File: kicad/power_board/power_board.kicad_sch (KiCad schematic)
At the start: 38 parts, among them J1 24V, J2 5V, J3 3V3, J4 GND, Q1 NTBGS1D5N06C, Q2 FDB13AN06A0, Q3 NTBGS1D5N06C, Q4 FDB13AN06A0, U1 LM2575D2T-3.3R4G, U2 LM2575D2T-5R4G, U3 LTC4359, U4 LTC4359

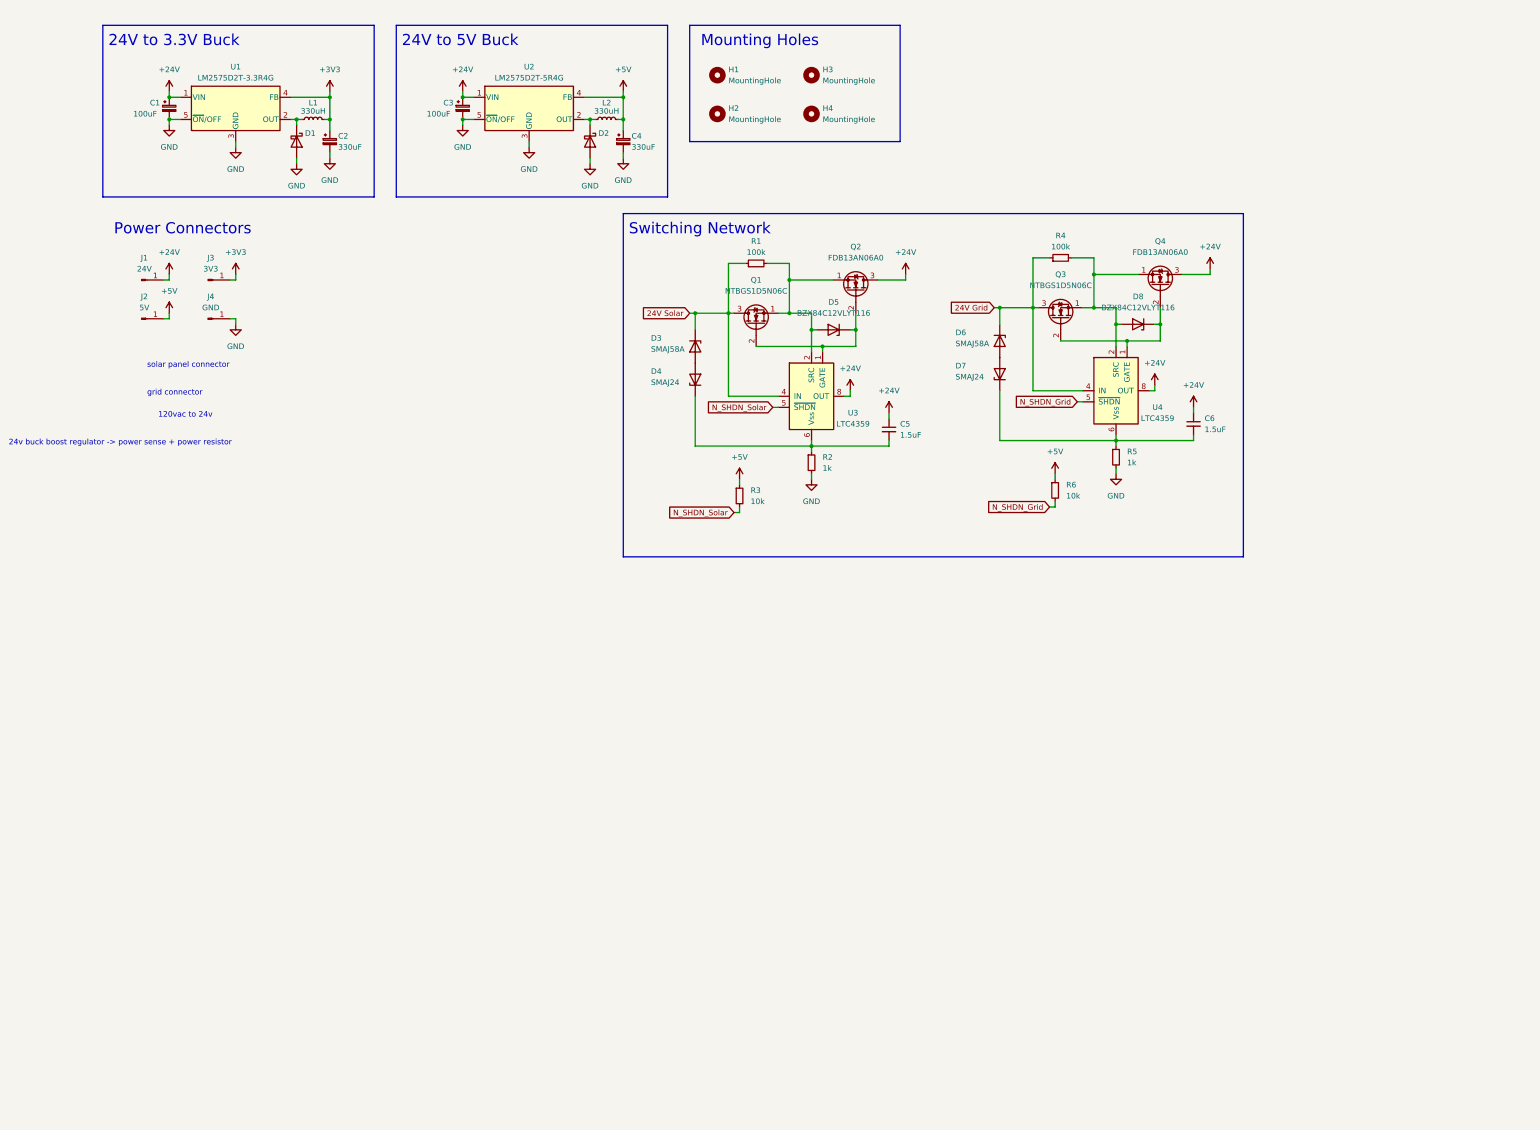
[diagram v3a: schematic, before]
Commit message: power board pcb
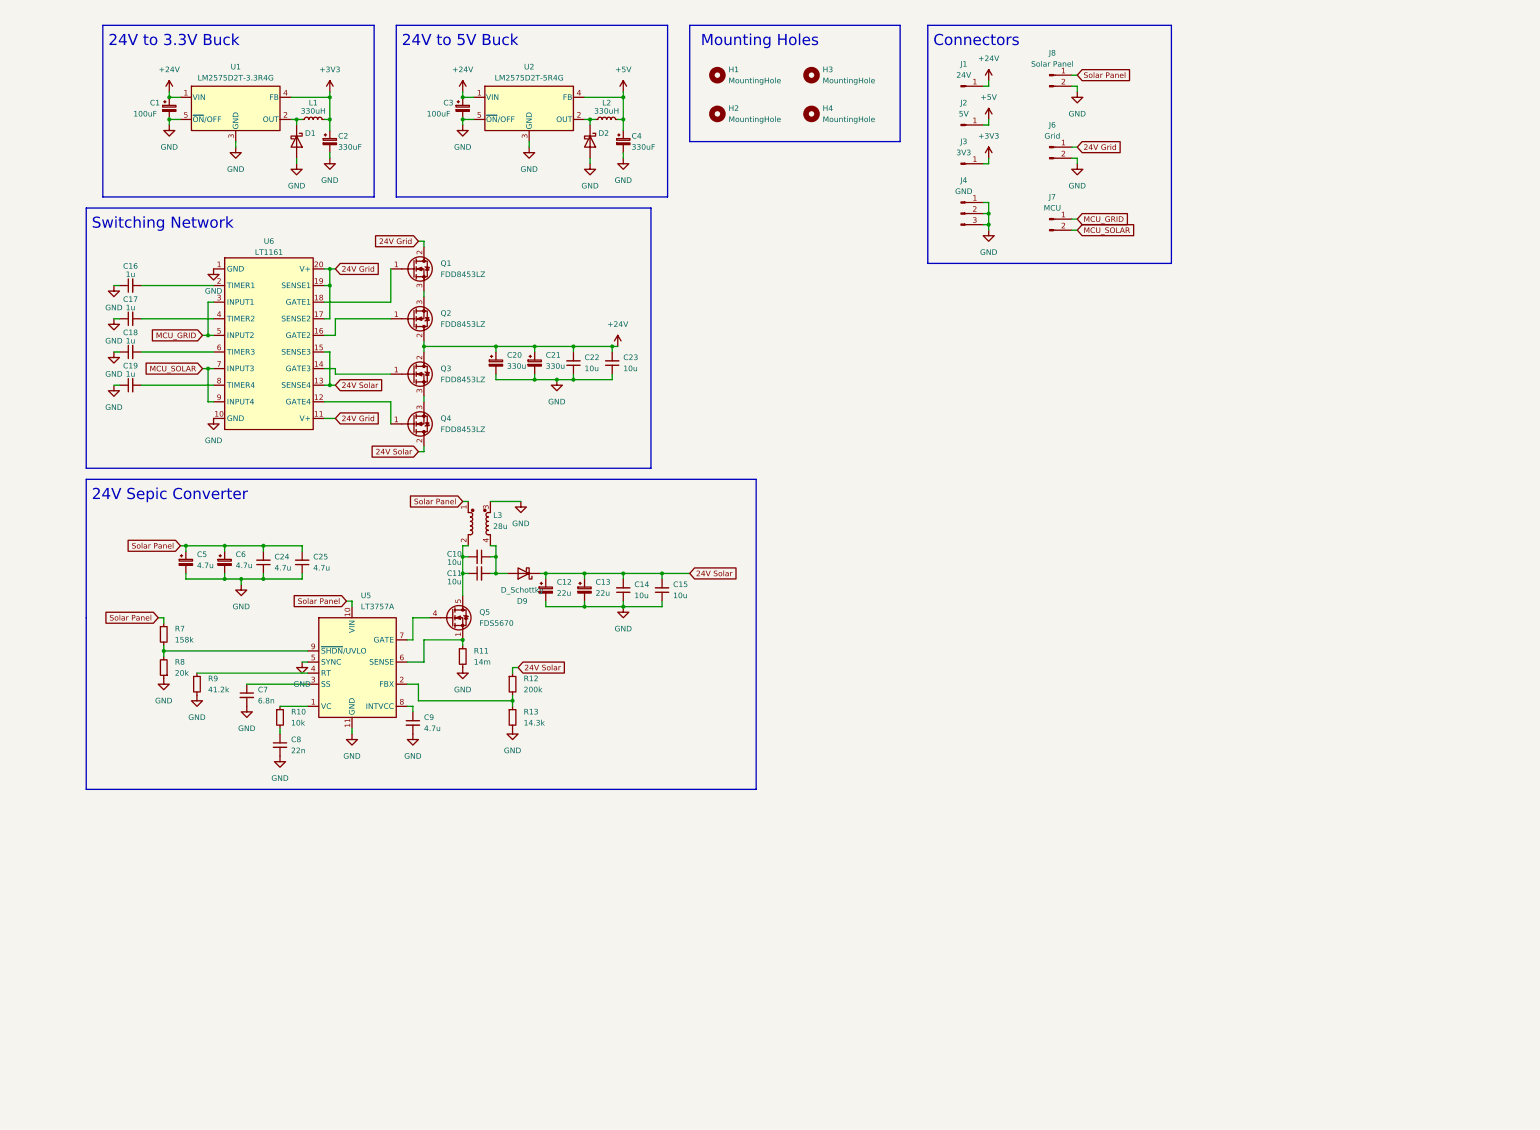
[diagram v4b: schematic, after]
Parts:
- removed C5, C6: 1.5uF, symbol Device:C_Small
- removed D3, D6: SMAJ58A, symbol Device:D_Zener
- removed D4, D7: SMAJ24, symbol Device:D_Zener
- removed D5, D8: BZX84C12VLYT116, symbol Device:D_Zener
- removed J4: GND, symbol Connector:Conn_01x01_Male
- removed Q1, Q3: NTBGS1D5N06C, Package_TO_SOT_THT:TO-92_Inline, symbol Transistor_FET:2N7000
- removed Q2, Q4: FDB13AN06A0, Package_TO_SOT_THT:TO-92_Inline, symbol Transistor_FET:2N7000
- removed R1, R4: 100k, symbol Device:R_Small
- removed R2, R5: 1k, symbol Device:R_Small
- removed R3, R6: 10k, symbol Device:R_Small
- removed U3, U4: LTC4359, Package_SO:MSOP-8_3x3mm_P0.65mm, symbol Power_Management:LTC4359-MS8
- added C10, C11, C14, C15, C22, C23: 10u, Capacitor_SMD:C_1210_3225Metric, symbol Device:C_Small
- added C12, C13: 22u, Capacitor_THT:CP_Radial_D5.0mm_P2.50mm, symbol Device:C_Polarized_Small
- added C16, C17, C18, C19: 1u, Capacitor_SMD:C_0603_1608Metric, symbol Device:C_Small
- added C20, C21: 330u, Capacitor_THT:C_Radial_D16.0mm_H25.0mm_P7.50mm, symbol Device:C_Polarized_Small
- added C24, C25: 4.7u, Capacitor_SMD:C_1210_3225Metric, symbol Device:C_Small
- added C5, C6: 4.7u, Capacitor_THT:CP_Radial_D5.0mm_P2.00mm, symbol Device:C_Polarized_Small
- added C7: 6.8n, Capacitor_SMD:C_0603_1608Metric, symbol Device:C_Small
- added C8: 22n, Capacitor_SMD:C_0603_1608Metric, symbol Device:C_Small
- added C9: 4.7u, Capacitor_SMD:C_0805_2012Metric, symbol Device:C_Small
- added D9: D_Schottky, Package_TO_SOT_SMD:TO-252-2, symbol Device:D_Schottky
- added J4: GND, Connector_PinHeader_2.54mm:PinHeader_1x03_P2.54mm_Vertical, symbol Connector:Conn_01x03_Male
- added J6: Grid, Connector_PinHeader_2.54mm:PinHeader_1x02_P2.54mm_Vertical, symbol Connector:Conn_01x02_Male
- added J7: MCU, Connector_PinHeader_2.54mm:PinHeader_1x02_P2.54mm_Vertical, symbol Connector:Conn_01x02_Male
- added J8: Solar Panel, Connector_PinHeader_2.54mm:PinHeader_1x02_P2.54mm_Vertical, symbol Connector:Conn_01x02_Male
- added L3: 28u, _mine:PF0553NL, symbol Device:L_Coupled
- added Q1, Q2, Q3, Q4: FDD8453LZ, Package_TO_SOT_SMD:TO-252-2, symbol Transistor_FET:BSP89
- added Q5: FDS5670, Package_TO_SOT_SMD:LFPAK33, symbol Transistor_FET:BUK7M6R3-40EX
- added R10: 10k, Resistor_SMD:R_0603_1608Metric, symbol Device:R_Small
- added R11: 14m, Resistor_SMD:R_2512_6332Metric, symbol Device:R_Small
- added R12: 200k, Resistor_SMD:R_1206_3216Metric, symbol Device:R_Small
- added R13: 14.3k, Resistor_SMD:R_0603_1608Metric, symbol Device:R_Small
- added R7: 158k, Resistor_SMD:R_0603_1608Metric, symbol Device:R_Small
- added R8: 20k, Resistor_SMD:R_0603_1608Metric, symbol Device:R_Small
- added R9: 41.2k, Resistor_SMD:R_0603_1608Metric, symbol Device:R_Small
- added U5: LT3757A, Package_SO:MSOP-10-1EP_3x3mm_P0.5mm_EP1.68x1.88mm, symbol Regulator_Switching:LT3757AEMSE
- added U6: LT1161, Package_SO:SOIC-20W_7.5x12.8mm_P1.27mm, symbol Driver_FET:HIP4080A
- C1, C3: footprint (none) -> Capacitor_THT:C_Radial_D8.0mm_H11.5mm_P3.50mm
- C2, C4: footprint (none) -> Capacitor_THT:CP_Radial_D8.0mm_P3.50mm
- D1, D2: footprint (none) -> Package_TO_SOT_SMD:TO-252-2
- H1, H2, H3, H4: footprint (none) -> MountingHole:MountingHole_3.5mm
- J1, J2, J3: footprint (none) -> Connector_PinHeader_2.54mm:PinHeader_1x01_P2.54mm_Vertical
- L1, L2: footprint (none) -> Inductor_THT:L_Toroid_Vertical_L31.8mm_W15.9mm_P13.50mm_Bourns_5700
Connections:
- net +24V: now also C20.1, C21.1, C22.2, C23.2, Q2.2 (D), Q3.2 (D)
- net 24V Grid: now also J6.1 (Pin_1), Q1.2 (D), U6.11 (V+), U6.17 (SENSE2), U6.19 (SENSE1), U6.20 (V+)
- net 24V Solar: now also C12.1, C13.1, C14.2, C15.2, D9.2 (K), Q4.2 (D), R12.1, U6.13 (SENSE4), U6.15 (SENSE3)
- net GND: now also C12.2, C13.2, C14.1, C15.1, C16.1, C17.1, C18.1, C19.1, C20.2, C21.2, C22.1, C23.1, C24.1, C25.1, C5.2, C6.2, C7.2, C8.2, C9.2, J4.1 (Pin_1), J4.2 (Pin_2), J4.3 (Pin_3), J6.2 (Pin_2), J8.2 (Pin_2), L3.3, R11.2, R13.2, R8.1, R9.2, U5.11 (GND), U5.5 (SYNC), U6.1 (GND), U6.10 (GND)
- new net: R7.2, R8.2, U5.9 (~{SHDN}/UVLO)
- new net: C9.1, U5.8 (INTVCC)
- new net: C10.1, C11.2, D9.1 (A), L3.4
- new net: C10.2, C11.1, L3.2, Q5.5 (D)
- new net: Q5.1 (S), Q5.2 (S), Q5.3 (S), R11.1, U5.6 (SENSE)
- new net: Q5.4 (G), U5.7 (GATE)
- new net: Q1.1 (G), U6.18 (GATE1)
- new net: Q1.3 (S), Q2.3 (S)
- new net: C16.2, U6.2 (TIMER1)
- new net: Q4.1 (G), U6.12 (GATE4)
- new net: Q3.1 (G), U6.14 (GATE3)
- new net: Q2.1 (G), U6.16 (GATE2)
- new net: C17.2, U6.4 (TIMER2)
- new net: C18.2, U6.6 (TIMER3)
- new net: C19.2, U6.8 (TIMER4)
- new net: Q3.3 (S), Q4.3 (S)
- new net: R9.1, U5.4 (RT)
- new net: C7.1, U5.3 (SS)
- new net: R12.2, R13.1, U5.2 (FBX)
- new net: R10.1, U5.1 (VC)
- new net: C8.1, R10.2
- new net MCU_GRID: J7.1 (Pin_1), U6.3 (INPUT1), U6.5 (INPUT2)
- new net MCU_SOLAR: J7.2 (Pin_2), U6.7 (INPUT3), U6.9 (INPUT4)
- new net Solar Panel: C24.2, C25.2, C5.1, C6.1, J8.1 (Pin_1), L3.1, R7.1, U5.10 (VIN)
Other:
- note added: "24V Sepic Converter"
- note added: "Connectors"
- note removed: "120vac to 24v"
- note removed: "24v buck boost regulator -> power sense + power resistor"
- note removed: "Power Connectors"
- note removed: "grid connector"
- note removed: "solar panel connector"
- moved on the sheet: J1, J2, J3

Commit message: traffic lights WIP
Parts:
- removed C1, C3: 100uF, Capacitor_THT:C_Radial_D8.0mm_H11.5mm_P3.50mm, symbol Device:C_Polarized_Small
- removed C2, C4: 330uF, Capacitor_THT:CP_Radial_D8.0mm_P3.50mm, symbol Device:C_Polarized_Small
- removed D1, D2: VS-30WQ04FNTR-M3, Package_TO_SOT_SMD:TO-252-2, symbol Device:D_Schottky
- removed J4: GND, Connector_PinHeader_2.54mm:PinHeader_1x03_P2.54mm_Vertical, symbol Connector:Conn_01x03_Male
- removed J6: Grid, Connector_PinHeader_2.54mm:PinHeader_1x02_P2.54mm_Vertical, symbol Connector:Conn_01x02_Male
- removed J8: Solar Panel, Connector_PinHeader_2.54mm:PinHeader_1x02_P2.54mm_Vertical, symbol Connector:Conn_01x02_Male
- removed L1, L2: 330uH, Inductor_THT:L_Toroid_Vertical_L31.8mm_W15.9mm_P13.50mm_Bourns_5700, symbol Device:L_Small
- removed U1: LM2575D2T-3.3R4G, Package_TO_SOT_SMD:TO-263-5_TabPin3, symbol Regulator_Switching:LM2575-3.3BU
- removed U2: LM2575D2T-5R4G, Package_TO_SOT_SMD:TO-263-5_TabPin3, symbol Regulator_Switching:LM2575-5.0BU
- added D1: LED, Capacitor_SMD:C_0603_1608Metric, symbol Device:LED
- added J10: Grid, Connector_PinHeader_2.54mm:PinHeader_1x01_P2.54mm_Vertical, symbol Connector:Conn_01x01_Male
- added J11: 24V Solar, Connector_PinHeader_2.54mm:PinHeader_1x01_P2.54mm_Vertical, symbol Connector:Conn_01x01_Male
- added J4, J5, J6: GND, Connector_PinHeader_2.54mm:PinHeader_1x01_P2.54mm_Vertical, symbol Connector:Conn_01x01_Male
- added J8: GND, _mine:73099, symbol Connector:Conn_01x01_Male
- added J9: Solar Panel, _mine:73099, symbol Connector:Conn_01x01_Male
- added R1: 1k, Resistor_SMD:R_2512_6332Metric, symbol Device:R_Small
- J2: value 5V -> 24V
- J3: value 3V3 -> GND
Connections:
- net +3V3 is gone; now on net GND: J3.1 (Pin_1)
- net +5V is gone; now on net +24V: J2.1 (Pin_1)
- net +24V: now also D1.2 (A)
- net 24V Grid: now also J10.1 (Pin_1)
- net 24V Solar: now also J11.1 (Pin_1)
- net GND: now also J4.1 (Pin_1), J5.1 (Pin_1), J6.1 (Pin_1), J8.1 (Pin_1), R1.2
- net Solar Panel: now also J9.1 (Pin_1)
- new net: D1.1 (K), R1.1
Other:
- note added: "Status LED"
- note removed: "24V to 3.3V Buck"
- note removed: "24V to 5V Buck"
- moved on the sheet: C10, C11, C12, C13, C14, C15, C16, C17, C18, C19, C20, C21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

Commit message: light board done
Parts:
- added J12: MCU_2, Connector_PinHeader_2.54mm:PinHeader_1x02_P2.54mm_Vertical, symbol Connector:Conn_01x02_Male
- added J13: GND, Connector_PinHeader_2.54mm:PinHeader_1x01_P2.54mm_Vertical, symbol Connector:Conn_01x01_Male
- added R2: 0.02, Resistor_SMD:R_0603_1608Metric, symbol Device:R_Small
- added R3, R4, R5, R6: 0, Resistor_SMD:R_2512_6332Metric, symbol Device:R_Small
- added U1: LTC4151xMS, Package_SO:MSOP-10_3x3mm_P0.5mm, symbol Analog_ADC:LTC4151xMS
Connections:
- net 24V Solar: now also R2.2, R3.1, R5.1, U1.1 (SENSE+), U1.2 (VIN); no longer J11.1 (Pin_1), Q4.2 (D), U6.13 (SENSE4), U6.15 (SENSE3)
- net GND: now also J13.1 (Pin_1), R4.2, R6.2, U1.5 (ADIN), U1.9 (GND)
- new net: R3.2, R4.1, U1.4 (ADR0)
- new net: R5.2, R6.1, U1.3 (ADR1)
- new net 24V Solar_2: J11.1 (Pin_1), Q4.2 (D), R2.1, U1.10 (SENSE-), U6.13 (SENSE4), U6.15 (SENSE3)
- new net MCU_SCL: J12.1 (Pin_1), U1.6 (SCL)
- new net MCU_SDA: J12.2 (Pin_2), U1.7 (SDA)
- no-connect marks 0 -> 1
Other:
- note added: "Power monitor"
- moved on the sheet: J11
